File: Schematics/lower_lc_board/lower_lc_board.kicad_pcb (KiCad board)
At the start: 2 copper layers, 69.5 x 60 mm, 130 parts, among them J1 Stack Male Edge Connector, J3 USB_C_CONN, J7 Screw_Terminal_01x02, Q1 AO3400A, Q2 AO3400A, SW1 SW_STM_RESET, SW2 SW_STM_BOOT_MODE, U1 TVS3300DRV, U10 ID_LM66100DCKR, U2 LD1117S33TR_SOT223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

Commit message: start layout
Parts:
- added C45: 0.1uF, Capacitor_SMD:C_0805_2012Metric, F.Cu at (90.9, 62.6)
- added F1: Fuse, 0679L0250-05:FUSC6125X279N, F.Cu at (101.3, 63.4)
- added J10: SOL_CONN, S02B_PASK_2:CONN2_S02B-PASK-2_JST, F.Cu at (181.2, 98.8)
- added J4: HALL-1, S04B_PASK_2:CONN4_S04B-PASK_JST, F.Cu at (135.7, 98.8)
- added J5: HALL-2, S04B_PASK_2:CONN4_S04B-PASK_JST, F.Cu at (147.2, 98.8)
- added J6: PT1, S02B_PASK_2:CONN2_S02B-PASK-2_JST, B.Cu at (131.6, 88.5)
- added J8: PT1, S02B_PASK_2:CONN2_S02B-PASK-2_JST, B.Cu at (139.2, 88.5)
- added J9: SOL_CONN, S02B_PASK_2:CONN2_S02B-PASK-2_JST, F.Cu at (174.0, 98.8)
- added TP7: USB-DM, TestPoint:TestPoint_Pad_D1.5mm, F.Cu at (86.9, 62.9)
- added TP8: USB-DP, TestPoint:TestPoint_Pad_D1.5mm, F.Cu at (86.9, 66.5)
- added U7: ISO1044BDR, ul_ISO1044BDR:SOIC_1044BDR_TEX, F.Cu at (133.2, 61.0)
- added U9: ADC_ADS131M04IPWR, ADS131M04IPWR:SOP65P640X120-20N, F.Cu at (144.3, 77.7)
- D11, D12: footprint Resistor_SMD:R_0603_1608Metric -> LED_SMD:LED_0603_1608Metric
- J7: moved to B.Cu
- R4: value 150 -> 330
- moved D16 148.6 mm to (180.3, 92.9), turned to 180 degrees
- moved D4 140.6 mm to (162.3, 99.8), turned to 90 degrees
- moved R4 140.4 mm to (159.6, 97.4)
- moved D15 138.6 mm to (172.9, 92.9), turned to 180 degrees
- moved J7 131.3 mm to (148.6, 88.5), turned to 180 degrees
- moved R31 106.5 mm to (168.0, 101.7), turned to 90 degrees
- moved R30 105.0 mm to (164.8, 101.7), turned to 90 degrees
- moved U6 104.1 mm to (165.3, 64.1)
- moved D12 101.9 mm to (168.0, 106.5)
- moved D11 99.9 mm to (164.6, 106.5)
- moved U5 58.5 mm to (153.8, 70.0)
- moved J3 55.5 mm to (155.8, 101.8)
- moved U8 25.1 mm to (109.1, 72.5)
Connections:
- net MISO renamed FL_MISO
- net MOSI renamed FL_MOSI
- net SCK renamed FL_SCK
- R4 pad 1: /Power Circuitry/3V3_USB -> 5V_USB
- U5 pad 10: unconnected-(U5-PA0-Pad10) -> ADC_DRDY
- U5 pad 11: FAULT_LED -> ADC_CLKIN
- U5 pad 12: PT_LED -> FL_CS
- U5 pad 13: TC_LED -> ADC_CS
- U5 pad 14: HALL_LED -> TEMP_SENSE
- U5 pad 15: FL_CS -> ADC_SCLK
- U5 pad 16: ADC_CS -> ADC_MISO
- U5 pad 17: TEMP_SENSE -> ADC_MOSI
- U5 pad 21: USB_RX -> USART-TX
- U5 pad 22: USB_TX -> USART-RX
- U5 pad 30: VALVE2_CTRL -> FAULT_LED
- U5 pad 31: ADC_DREADY -> VALVE2_CTRL
- U5 pad 32: unconnected-(U5-PA11-Pad32) -> Net-(U5-PA11)
- U5 pad 33: unconnected-(U5-PA12-Pad33) -> Net-(U5-PA12)
- U5 pad 38: ADC_CLKIN -> unconnected-(U5-PA15-Pad38)
- U8 pad 25: USB_TX -> USART_TX
- U8 pad 26: USB_RX -> USART_RX

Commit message: replace sensing LEDs with a single
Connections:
- R21 pad 1: PT_LED -> SENS_LED
- U5 pad 41: unconnected-(U5-PB5-Pad41) -> SENS_LED
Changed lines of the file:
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@@
 	(net 73 "HALL_SDA")
 	(net 74 "HALL_SCL")
-	(net 75 "PT_LED")
+	(net 75 "SENS_LED")
 	(net 76 "TC_LED")
 	(net 77 "HALL_LED")
@@
 	(net 105 "FL_CS")
 	(net 106 "unconnected-(U5-PC15-Pad4)")
-	(net 107 "unconnected-(U5-PB5-Pad41)")
-	(net 108 "CAN_TX")
-	(net 109 "unconnected-(U8-~{CTS}-Pad23)")
-	(net 110 "unconnected-(U8-GPIO.5-Pad21)")
-	(net 111 "unconnected-(U8-~{DSR}-Pad27)")
-	(net 112 "unconnected-(U8-~{DTR}-Pad28)")
-	(net 113 "unconnected-(U8-CHR0-Pad15)")
-	(net 114 "unconnected-(U8-~{DCD}-Pad1)")
-	(net 115 "unconnected-(U8-~{RI}{slash}CLK-Pad2)")
-	(net 116 "unconnected-(U8-GPIO.4-Pad22)")
-	(net 117 "unconnected-(U8-~{TXT}{slash}GPIO.0-Pad19)")
-	(net 118 "unconnected-(U8-~{SUSPEND}-Pad11)")
-	(net 119 "unconnected-(U8-CHR1-Pad14)")
-	(net 120 "unconnected-(U8-~{RXT}{slash}GPIO.1-Pad18)")
-	(net 121 "unconnected-(U8-SUSPEND-Pad12)")
-	(net 122 "unconnected-(U8-~{RTS}-Pad24)")
-	(net 123 "unconnected-(U8-NC-Pad10)")
-	(net 124 "unconnected-(U8-~{WAKEUP}{slash}GPIO.3-Pad16)")
-	(net 125 "unconnected-(U8-GPIO.6-Pad20)")
-	(net 126 "unconnected-(U8-CHREN-Pad13)")
-	(net 127 "unconnected-(U8-RS485{slash}GPIO.2-Pad17)")
-	(net 128 "unconnected-(U10-NC-Pad4)")
-	(net 129 "USART_RX")
-	(net 130 "USART_TX")
-	(net 131 "ADC_SCLK")
-	(net 132 "ADC_MISO")
-	(net 133 "ADC_MOSI")
-	(net 134 "CAN_H")
-	(net 135 "CAN_L")
+	(net 107 "CAN_TX")
+	(net 108 "unconnected-(U8-~{CTS}-Pad23)")
+	(net 109 "unconnected-(U8-GPIO.5-Pad21)")
+	(net 110 "unconnected-(U8-~{DSR}-Pad27)")
+	(net 111 "unconnected-(U8-~{DTR}-Pad28)")
+	(net 112 "unconnected-(U8-CHR0-Pad15)")
+	(net 113 "unconnected-(U8-~{DCD}-Pad1)")
+	(net 114 "unconnected-(U8-~{RI}{slash}CLK-Pad2)")
+	(net 115 "unconnected-(U8-GPIO.4-Pad22)")
+	(net 116 "unconnected-(U8-~{TXT}{slash}GPIO.0-Pad19)")
+	(net 117 "unconnected-(U8-~{SUSPEND}-Pad11)")
+	(net 118 "unconnected-(U8-CHR1-Pad14)")
+	(net 119 "unconnected-(U8-~{RXT}{slash}GPIO.1-Pad18)")
+	(net 120 "unconnected-(U8-SUSPEND-Pad12)")
+	(net 121 "unconnected-(U8-~{RTS}-Pad24)")
+	(net 122 "unconnected-(U8-NC-Pad10)")
+	(net 123 "unconnected-(U8-~{WAKEUP}{slash}GPIO.3-Pad16)")
+	(net 124 "unconnected-(U8-GPIO.6-Pad20)")
+	(net 125 "unconnected-(U8-CHREN-Pad13)")
+	(net 126 "unconnected-(U8-RS485{slash}GPIO.2-Pad17)")
+	(net 127 "unconnected-(U10-NC-Pad4)")
+	(net 128 "USART_RX")
+	(net 129 "USART_TX")
+	(net 130 "ADC_SCLK")
+	(net 131 "ADC_MISO")
+	(net 132 "ADC_MOSI")
+	(net 133 "CAN_H")
+	(net 134 "CAN_L")
 	(footprint "Connector_PCBEdge:BUS_PCIexpress_x1"
 		(layer "F.Cu")
@@
 			(layers "F.Cu" "F.Paste" "F.Mask")
 			(roundrect_rratio 0.25)
-			(net 75 "PT_LED")
+			(net 75 "SENS_LED")
 			(pintype "passive")
 		)
@@
 			(layers "F.Cu" "F.Paste" "F.Mask")
 			(roundrect_rratio 0.25)
-			(net 131 "ADC_SCLK")
+			(net 130 "ADC_SCLK")
 			(pinfunction "PA5")
 			(pintype "bidirectional")
@@
 			(layers "F.Cu" "F.Paste" "F.Mask")
 			(roundrect_rratio 0.25)
-			(net 132 "ADC_MISO")
+			(net 131 "ADC_MISO")
 			(pinfunction "PA6")
 			(pintype "bidirectional")
@@
 			(layers "F.Cu" "F.Paste" "F.Mask")
 			(roundrect_rratio 0.25)
-			(net 133 "ADC_MOSI")
+			(net 132 "ADC_MOSI")
 			(pinfunction "PA7")
 			(pintype "bidirectional")
@@
 			(layers "F.Cu" "F.Paste" "F.Mask")
 			(roundrect_rratio 0.25)
-			(net 107 "unconnected-(U5-PB5-Pad41)")
+			(net 75 "SENS_LED")
 			(pinfunction "PB5")
-			(pintype "bidirectional+no_connect")
+			(pintype "bidirectional")
 		)
 		(pad "42" smd roundrect
@@
 			(layers "F.Cu" "F.Paste" "F.Mask")
 			(roundrect_rratio 0.25)
-			(net 108 "CAN_TX")
+			(net 107 "CAN_TX")
 			(pinfunction "PB9")
 			(pintype "bidirectional")
@@
 			(size 1.4605 0.5588)
 			(layers "F.Cu" "F.Paste" "F.Mask")
-			(net 108 "CAN_TX")
+			(net 107 "CAN_TX")
 			(pinfunction "TXD")
 			(pintype "input")
@@
 			(size 1.4605 0.5588)
 			(layers "F.Cu" "F.Paste" "F.Mask")
-			(net 135 "CAN_L")
+			(net 134 "CAN_L")
 			(pinfunction "CANL")
 			(pintype "bidirectional")
@@
 			(size 1.4605 0.5588)
 			(layers "F.Cu" "F.Paste" "F.Mask")
-			(net 134 "CAN_H")
+			(net 133 "CAN_H")
 			(pinfunction "CANH")
 			(pintype "bidirectional")
@@
 			(layers "F.Cu" "F.Paste" "F.Mask")
 			(roundrect_rratio 0.125)
-			(net 131 "ADC_SCLK")
+			(net 130 "ADC_SCLK")
 			(pinfunction "SCLK")
 			(pintype "input")
@@
 			(layers "F.Cu" "F.Paste" "F.Mask")
 			(roundrect_rratio 0.125)
-			(net 132 "ADC_MISO")
+			(net 131 "ADC_MISO")
 			(pinfunction "DOUT")
 			(pintype "output")
@@
 			(layers "F.Cu" "F.Paste" "F.Mask")
 			(roundrect_rratio 0.125)
-			(net 133 "ADC_MOSI")
+			(net 132 "ADC_MOSI")
 			(pinfunction "DIN")
 			(pintype "input")
@@
 			(layers "F.Cu" "F.Paste" "F.Mask")
 			(roundrect_rratio 0.25)
-			(net 114 "unconnected-(U8-~{DCD}-Pad1)")
+			(net 113 "unconnected-(U8-~{DCD}-Pad1)")
 			(pinfunction "~{DCD}")
 			(pintype "input+no_connect")
@@
 			(layers "F.Cu" "F.Paste" "F.Mask")
 			(roundrect_rratio 0.25)
-			(net 115 "unconnected-(U8-~{RI}{slash}CLK-Pad2)")
+			(net 114 "unconnected-(U8-~{RI}{slash}CLK-Pad2)")
 			(pinfunction "~{RI}/CLK")
 			(pintype "bidirectional+no_connect")
@@
 			(layers "F.Cu" "F.Paste" "F.Mask")
 			(roundrect_rratio 0.25)
-			(net 123 "unconnected-(U8-NC-Pad10)")
+			(net 122 "unconnected-(U8-NC-Pad10)")
 			(pinfunction "NC")
 			(pintype "no_connect")
@@
 			(layers "F.Cu" "F.Paste" "F.Mask")
 			(roundrect_rratio 0.25)
-			(net 118 "unconnected-(U8-~{SUSPEND}-Pad11)")
+			(net 117 "unconnected-(U8-~{SUSPEND}-Pad11)")
 			(pinfunction "~{SUSPEND}")
 			(pintype "output+no_connect")
@@
 			(layers "F.Cu" "F.Paste" "F.Mask")
 			(roundrect_rratio 0.25)
-			(net 121 "unconnected-(U8-SUSPEND-Pad12)")
+			(net 120 "unconnected-(U8-SUSPEND-Pad12)")
 			(pinfunction "SUSPEND")
 			(pintype "output+no_connect")
@@
 			(layers "F.Cu" "F.Paste" "F.Mask")
 			(roundrect_rratio 0.25)
-			(net 126 "unconnected-(U8-CHREN-Pad13)")
+			(net 125 "unconnected-(U8-CHREN-Pad13)")
 			(pinfunction "CHREN")
 			(pintype "output+no_connect")
@@
 			(layers "F.Cu" "F.Paste" "F.Mask")
 			(roundrect_rratio 0.25)
-			(net 119 "unconnected-(U8-CHR1-Pad14)")
+			(net 118 "unconnected-(U8-CHR1-Pad14)")
 			(pinfunction "CHR1")
 			(pintype "output+no_connect")
@@
 			(layers "F.Cu" "F.Paste" "F.Mask")
 			(roundrect_rratio 0.25)
-			(net 113 "unconnected-(U8-CHR0-Pad15)")
+			(net 112 "unconnected-(U8-CHR0-Pad15)")
 			(pinfunction "CHR0")
 			(pintype "output+no_connect")
@@
 			(layers "F.Cu" "F.Paste" "F.Mask")
 			(roundrect_rratio 0.25)
-			(net 124 "unconnected-(U8-~{WAKEUP}{slash}GPIO.3-Pad16)")
+			(net 123 "unconnected-(U8-~{WAKEUP}{slash}GPIO.3-Pad16)")
 			(pinfunction "~{WAKEUP}/GPIO.3")
 			(pintype "bidirectional+no_connect")
@@
 			(layers "F.Cu" "F.Paste" "F.Mask")
 			(roundrect_rratio 0.25)
-			(net 127 "unconnected-(U8-RS485{slash}GPIO.2-Pad17)")
+			(net 126 "unconnected-(U8-RS485{slash}GPIO.2-Pad17)")
 			(pinfunction "RS485/GPIO.2")
 			(pintype "bidirectional+no_connect")
@@
 			(layers "F.Cu" "F.Paste" "F.Mask")
 			(roundrect_rratio 0.25)
-			(net 120 "unconnected-(U8-~{RXT}{slash}GPIO.1-Pad18)")
+			(net 119 "unconnected-(U8-~{RXT}{slash}GPIO.1-Pad18)")
 			(pinfunction "~{RXT}/GPIO.1")
 			(pintype "bidirectional+no_connect")
@@
 			(layers "F.Cu" "F.Paste" "F.Mask")
 			(roundrect_rratio 0.25)
-			(net 117 "unconnected-(U8-~{TXT}{slash}GPIO.0-Pad19)")
+			(net 116 "unconnected-(U8-~{TXT}{slash}GPIO.0-Pad19)")
 			(pinfunction "~{TXT}/GPIO.0")
 			(pintype "bidirectional+no_connect")
@@
 			(layers "F.Cu" "F.Paste" "F.Mask")
 			(roundrect_rratio 0.25)
-			(net 125 "unconnected-(U8-GPIO.6-Pad20)")
+			(net 124 "unconnected-(U8-GPIO.6-Pad20)")
 			(pinfunction "GPIO.6")
 			(pintype "bidirectional+no_connect")
@@
 			(layers "F.Cu" "F.Paste" "F.Mask")
 			(roundrect_rratio 0.25)
-			(net 110 "unconnected-(U8-GPIO.5-Pad21)")
+			(net 109 "unconnected-(U8-GPIO.5-Pad21)")
 			(pinfunction "GPIO.5")
 			(pintype "bidirectional+no_connect")
@@
 			(layers "F.Cu" "F.Paste" "F.Mask")
 			(roundrect_rratio 0.25)
-			(net 116 "unconnected-(U8-GPIO.4-Pad22)")
+			(net 115 "unconnected-(U8-GPIO.4-Pad22)")
 			(pinfunction "GPIO.4")
 			(pintype "bidirectional+no_connect")
@@
 			(layers "F.Cu" "F.Paste" "F.Mask")
 			(roundrect_rratio 0.25)
-			(net 109 "unconnected-(U8-~{CTS}-Pad23)")
+			(net 108 "unconnected-(U8-~{CTS}-Pad23)")
 			(pinfunction "~{CTS}")
 			(pintype "input+no_connect")
@@
 			(layers "F.Cu" "F.Paste" "F.Mask")
 			(roundrect_rratio 0.25)
-			(net 122 "unconnected-(U8-~{RTS}-Pad24)")
+			(net 121 "unconnected-(U8-~{RTS}-Pad24)")
 			(pinfunction "~{RTS}")
 			(pintype "output+no_connect")
@@
 			(layers "F.Cu" "F.Paste" "F.Mask")
 			(roundrect_rratio 0.25)
-			(net 130 "USART_TX")
+			(net 129 "USART_TX")
 			(pinfunction "RXD")
 			(pintype "input")
@@
 			(layers "F.Cu" "F.Paste" "F.Mask")
 			(roundrect_rratio 0.25)
-			(net 129 "USART_RX")
+			(net 128 "USART_RX")
 			(pinfunction "TXD")
 			(pintype "output")
@@
 			(layers "F.Cu" "F.Paste" "F.Mask")
 			(roundrect_rratio 0.25)
-			(net 111 "unconnected-(U8-~{DSR}-Pad27)")
+			(net 110 "unconnected-(U8-~{DSR}-Pad27)")
 			(pinfunction "~{DSR}")
 			(pintype "input+no_connect")
@@
 			(layers "F.Cu" "F.Paste" "F.Mask")
 			(roundrect_rratio 0.25)
-			(net 112 "unconnected-(U8-~{DTR}-Pad28)")
+			(net 111 "unconnected-(U8-~{DTR}-Pad28)")
 			(pinfunction "~{DTR}")
 			(pintype "output+no_connect")
@@
 			(size 0.3 1)
 			(layers "F.Cu" "F.Paste" "F.Mask")
-			(net 128 "unconnected-(U10-NC-Pad4)")
+			(net 127 "unconnected-(U10-NC-Pad4)")
 			(pinfunction "NC")
 			(pintype "no_connect")

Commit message: quick changes
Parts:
- moved U8 53.3 mm to (159.8, 88.9)
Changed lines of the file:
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@@
 			)
 		)
+		(model "C:/Users/jeeva/Documents/GitHub/propulsion-integration/Schematics/upper_lc_board/models/S02B-PASK-2.stp"
+			(offset
+				(xyz -2 8 0)
+			)
+			(scale
+				(xyz 1 1 1)
+			)
+			(rotate
+				(xyz -90 0 -180)
+			)
+		)
 	)
 	(footprint "Capacitor_SMD:C_0402_1005Metric"
@@
 			)
 		)
+		(model "C:/Users/jeeva/Documents/GitHub/propulsion-integration/Schematics/upper_lc_board/models/S02B-PASK-2.stp"
+			(offset
+				(xyz -2 8.5 0)
+			)
+			(scale
+				(xyz 1 1 1)
+			)
+			(rotate
+				(xyz -90 0 -180)
+			)
+		)
 	)
 	(footprint "Capacitor_SMD:C_0603_1608Metric"
@@
 			)
 		)
+		(model "C:/Users/jeeva/Documents/GitHub/propulsion-integration/Schematics/upper_lc_board/models/S04B-PASK-2.STEP"
+			(offset
+				(xyz 3 2.5 0)
+			)
+			(scale
+				(xyz 1 1 1)
+			)
+			(rotate
+				(xyz -90 0 0)
+			)
+		)
 	)
 	(footprint "Resistor_SMD:R_1206_3216Metric_Pad1.30x1.75mm_HandSolder"
@@
 			)
 		)
+		(model "C:/Users/jeeva/Documents/GitHub/propulsion-integration/Schematics/upper_lc_board/models/S04B-PASK-2.STEP"
+			(offset
+				(xyz 3 2.5 0)
+			)
+			(scale
+				(xyz 1 1 1)
+			)
+			(rotate
+				(xyz -90 0 0)
+			)
+		)
 	)
 	(footprint "Capacitor_SMD:CP_Elec_6.3x5.9"
@@
 			)
 		)
+		(model "C:/Users/jeeva/Documents/GitHub/propulsion-integration/Schematics/upper_lc_board/models/ISO1042BDWVR.step"
+			(offset
+				(xyz 0 0 0)
+			)
+			(scale
+				(xyz 1 1 1)
+			)
+			(rotate
+				(xyz -90 0 0)
+			)
+		)
 	)
 	(footprint "Capacitor_SMD:C_0603_1608Metric"
@@
 			)
 		)
+		(model "C:/Users/jeeva/Documents/GitHub/propulsion-integration/Schematics/upper_lc_board/models/ADS131M04IPWR.step"
+			(offset
+				(xyz 0 0 0)
+			)
+			(scale
+				(xyz 1 1 1)
+			)
+			(rotate
+				(xyz -90 0 0)
+			)
+		)
 	)
 	(footprint "Resistor_SMD:R_0603_1608Metric_Pad0.98x0.95mm_HandSolder"
@@
 	(footprint "Package_DFN_QFN:QFN-28-1EP_5x5mm_P0.5mm_EP3.35x3.35mm"
 		(layer "F.Cu")
-		(at 109.07 72.54)
+		(at 159.75 88.9)
 		(descr "QFN, 28 Pin (http://ww1.microchip.com/downloads/en/PackagingSpec/00000049BQ.pdf#page=283), generated with kicad-footprint-generator ipc_noLead_generator.py")
 		(tags "QFN NoLead")
@@
 			)
 		)
+		(model "C:/Users/jeeva/Documents/GitHub/propulsion-integration/Schematics/upper_lc_board/models/S02B-PASK-2.stp"
+			(offset
+				(xyz -2 8.5 0)
+			)
+			(scale
+				(xyz 1 1 1)
+			)
+			(rotate
+				(xyz -90 0 -180)
+			)
+		)
 	)
 	(footprint "S02B_PASK_2:CONN2_S02B-PASK-2_JST"
@@
 			)
 			(scale
+				(xyz 1 1 1)
+			)
+			(rotate
+				(xyz -90 0 -180)
+			)
+		)
+		(model "C:/Users/jeeva/Documents/GitHub/propulsion-integration/Schematics/upper_lc_board/models/S02B-PASK-2.stp"
+			(offset
+				(xyz -2 8.5 0)
+			)
+			(scale

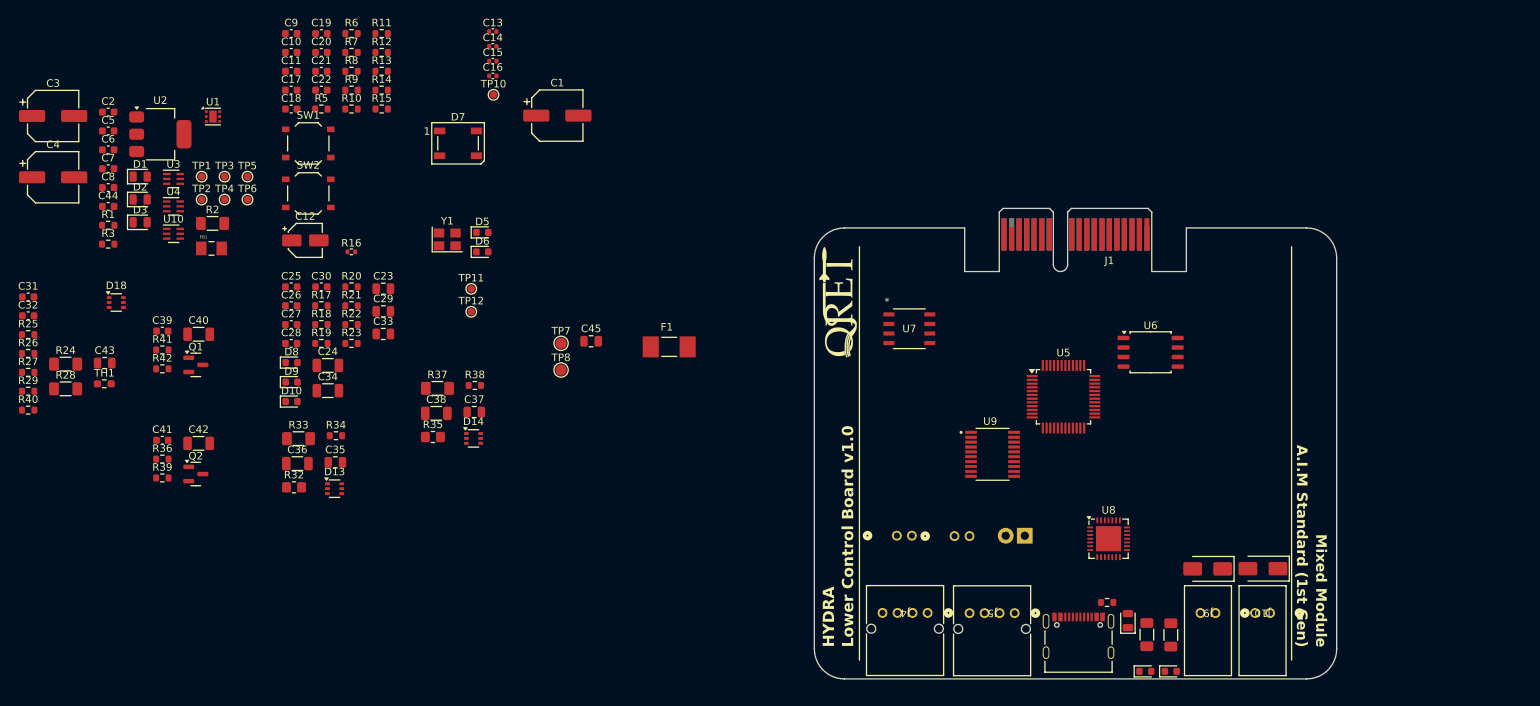
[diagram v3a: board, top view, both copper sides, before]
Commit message: layout work
#TODO
- smaller 3V3 buck, add HF cap
- finish layout
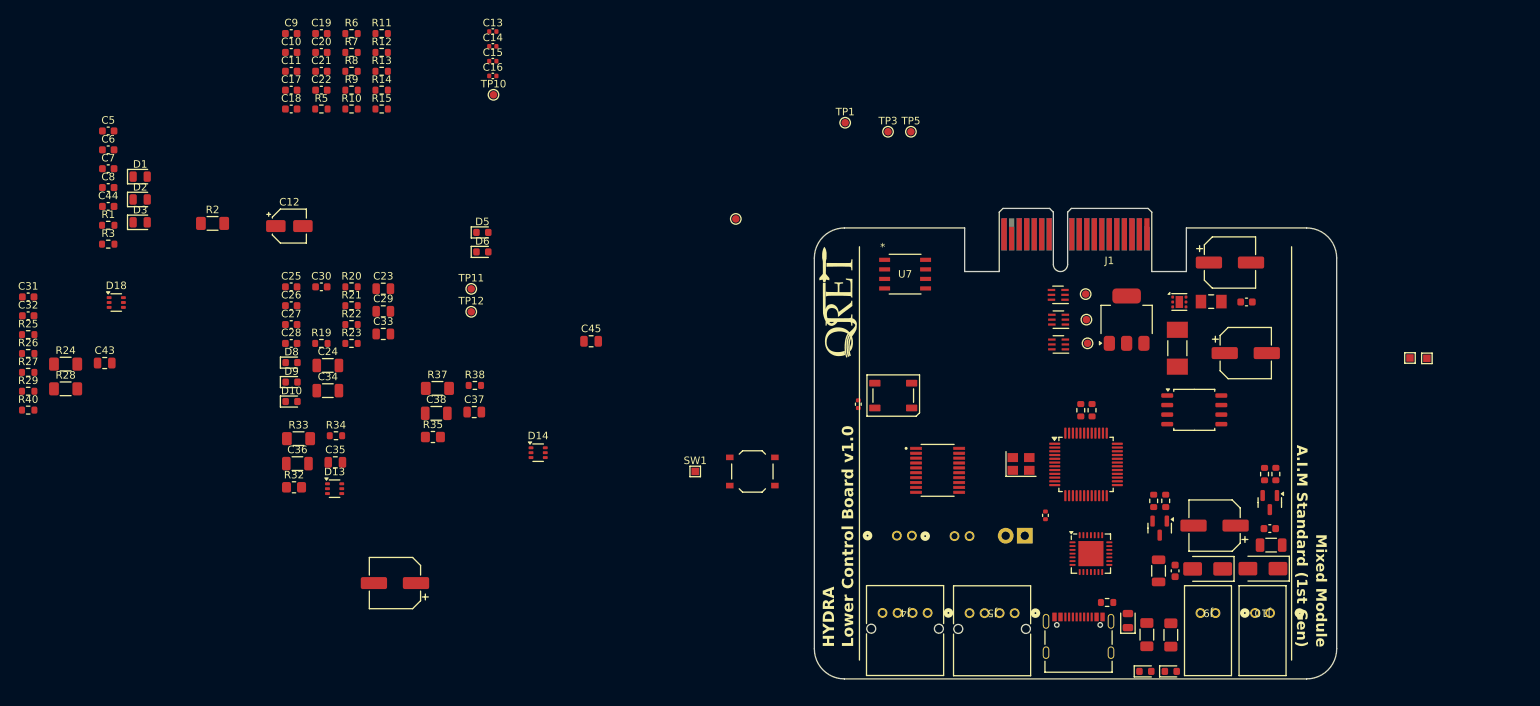
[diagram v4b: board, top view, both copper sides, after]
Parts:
- added C46: 100uF 50V, Capacitor_SMD:CP_Elec_6.3x5.9, F.Cu at (173.8, 87.2)
- added TP9: V_SWD_TP, TestPoint:TestPoint_Pad_D1.0mm, F.Cu at (156.9, 62.9)
- SW1: footprint Button_Switch_SMD:SW_Push_1P1T_XKB_TS-1187A -> TestPoint:TestPoint_Pad_1.0x1.0mm
- TH1: footprint Resistor_SMD:R_0603_1608Metric_Pad0.98x0.95mm_HandSolder -> Resistor_SMD:R_0402_1005Metric
- TP7, TP8: footprint TestPoint:TestPoint_Pad_D1.5mm -> TestPoint:TestPoint_Pad_1.0x1.0mm
- moved C4 160.4 mm to (178.0, 64.2)
- moved C3 157.8 mm to (175.9, 52.1)
- moved C2 153.5 mm to (178.1, 57.4)
- moved C39 149.7 mm to (181.2, 87.5)
- moved R39 148.2 mm to (182.0, 80.3), turned to -90 degrees
- moved R36 146.7 mm to (180.5, 80.3), turned to 90 degrees
- moved C40 145.4 mm to (181.4, 89.8)
- moved Q2 143.0 mm to (181.2, 84.1), turned to -90 degrees
- moved C41 135.9 mm to (168.6, 93.2), turned to 90 degrees
- moved R42 134.7 mm to (167.3, 83.9), turned to 90 degrees
- moved R41 133.4 mm to (165.8, 83.9), turned to 90 degrees
- moved FB1 133.2 mm to (173.4, 57.4), turned to 180 degrees
- moved U1 130.9 mm to (169.2, 57.4)
- moved U2 130.9 mm to (162.2, 59.8), turned to 90 degrees
- moved Q1 130.1 mm to (166.6, 87.5), turned to -90 degrees
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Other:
- copper layers 2 -> 4

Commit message: layout work
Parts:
- removed D10, D9: LED, LED_SMD:LED_0603_1608Metric
- removed R22, R23: 150, Resistor_SMD:R_0603_1608Metric
- SW1: footprint TestPoint:TestPoint_Pad_1.0x1.0mm -> Button_Switch_SMD:SW_Push_1P1T_XKB_TS-1187A
- moved R3 153.0 mm to (178.3, 70.2), turned to 90 degrees
- moved D3 152.0 mm to (181.1, 69.6), turned to 180 degrees
- moved C1 151.0 mm to (210.6, 55.5)
- moved C8 129.3 mm to (154.8, 59.7), turned to 90 degrees
- moved C6 128.6 mm to (153.3, 59.7), turned to 90 degrees
- moved C5 128.5 mm to (153.3, 56.4), turned to -90 degrees
- moved C44 128.1 mm to (153.4, 63.2), turned to 90 degrees
- moved R14 121.5 mm to (174.2, 78.2), turned to -90 degrees
- moved R10 119.0 mm to (159.5, 95.5)
- moved R9 115.3 mm to (153.4, 95.5), turned to 180 degrees
- moved R1 114.6 mm to (140.2, 62.4), turned to -90 degrees
- moved D8 111.8 mm to (162.8, 70.0), turned to 180 degrees
- moved D1 108.0 mm to (136.7, 62.3)
- moved TP12 107.3 mm to (179.1, 84.9)
- moved D2 106.8 mm to (136.8, 57.6)
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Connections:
- U5 pad 21: USART-TX -> USART_TX
- U5 pad 22: USART-RX -> USART_RX
